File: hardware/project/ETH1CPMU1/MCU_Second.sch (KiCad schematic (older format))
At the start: 32 parts, among them J1601 Conn_02x05, U1601 24LC08B-E/MS, U1602 STM32H743ZI, U1603 MCP23S17_ML, Y1601 NX3225GD-8MHZ-STD-CRA-3

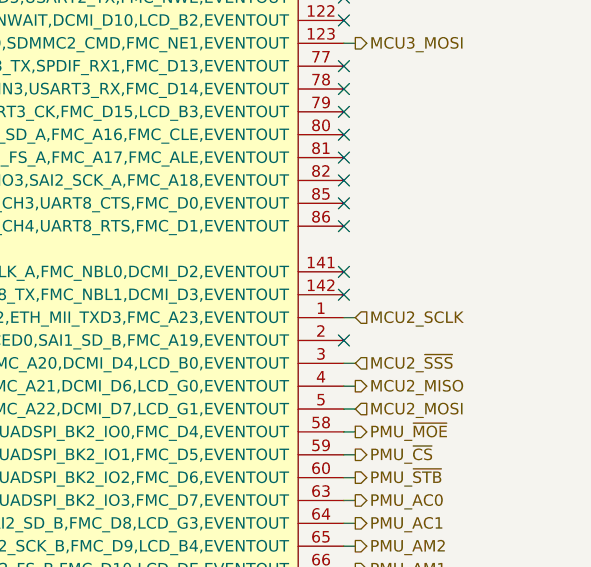
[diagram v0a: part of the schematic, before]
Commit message: Added two analog switches
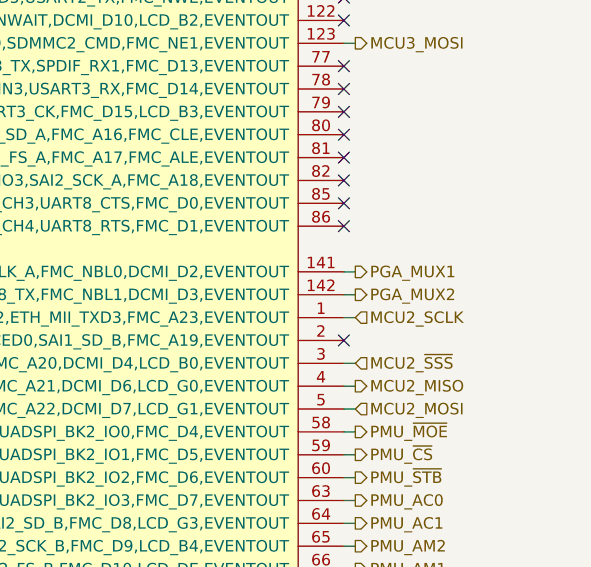
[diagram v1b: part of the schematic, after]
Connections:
- net PGA_MUX1: now reaches U1602.141 (PE0,TIM4_ETR,LPTIM1_ETR,UART8_RX,SAI2_MCLK_A,FMC_NBL0,DCMI_D2,EVENTOUT)
- net PGA_MUX2: now reaches U1602.142 (PE1,LPTIM1_IN2,UART8_TX,FMC_NBL1,DCMI_D3,EVENTOUT)
- no-connect marks 65 -> 63
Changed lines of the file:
@@
 NoConn ~ 15000 1450
 NoConn ~ 15000 3550
-NoConn ~ 15000 4650
-NoConn ~ 15000 4750
 NoConn ~ 15000 6650
 NoConn ~ 15000 6750
@@
 Text HLabel 15050 5950 2    50   Output ~ 0
 PMU_AM1
+Text HLabel 15050 4650 2    50   Output ~ 0
+PGA_MUX1
+Text HLabel 15050 4750 2    50   Output ~ 0
+PGA_MUX2
+Wire Wire Line
+	15000 4750 15050 4750
+Wire Wire Line
+	15050 4650 15000 4650
 $EndSCHEMATC
